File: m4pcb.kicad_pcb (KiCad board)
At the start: 2 copper layers, 26.4 x 82.3 mm, 5 parts, among them P1 CONN_01X16, P2 CONN_01X16, P3 CONN_01X16, P4 CONN_01X16, U1 STM32F415RG

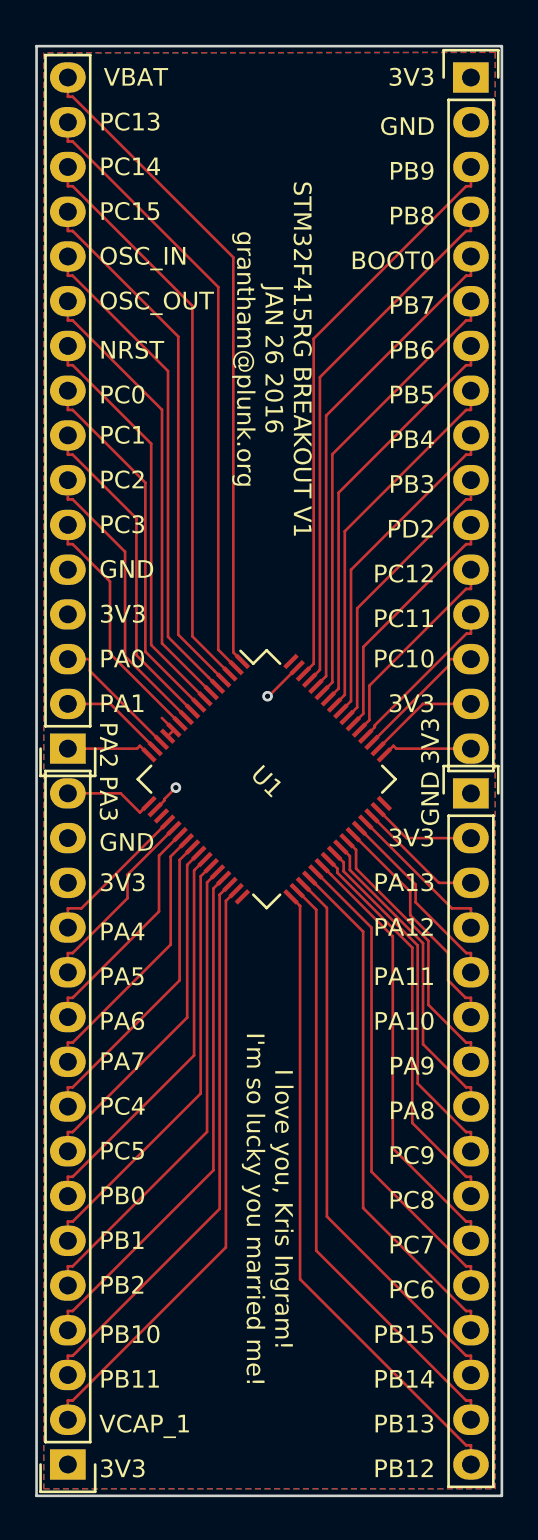
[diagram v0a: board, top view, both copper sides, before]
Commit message: narrower, would've been 2 at oshpark
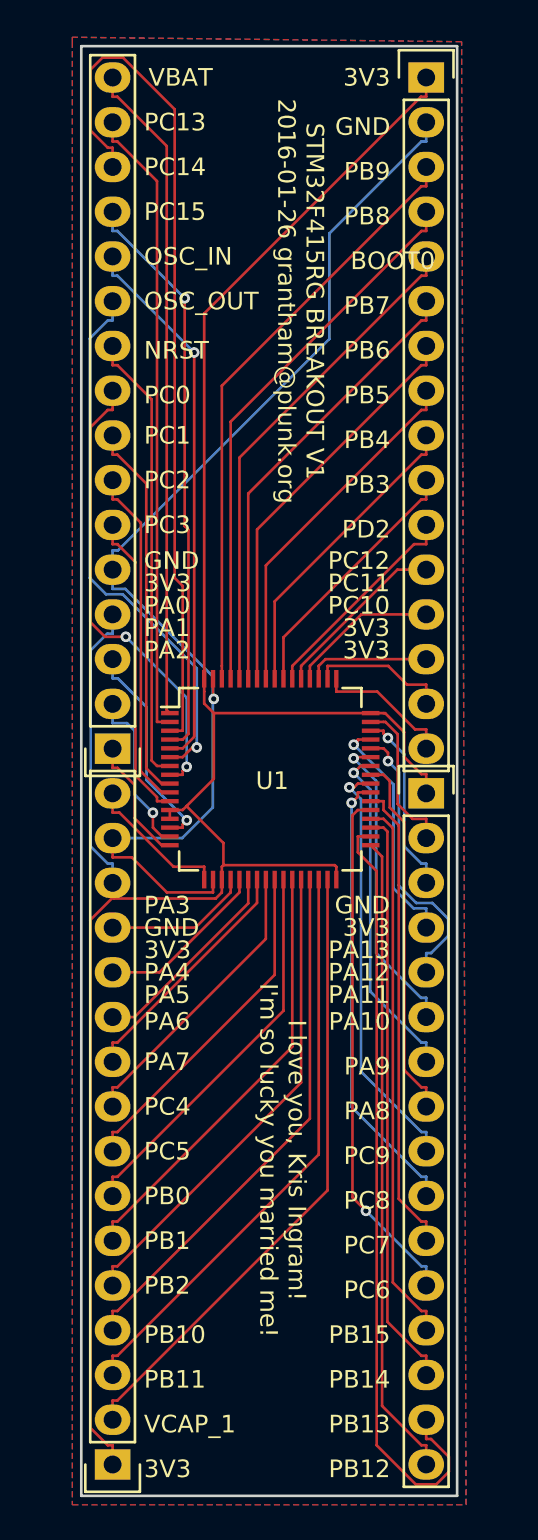
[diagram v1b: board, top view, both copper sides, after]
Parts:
- moved P1 2.54 mm to (118.1, 100.1)
- moved P2 2.54 mm to (118.1, 140.7)
- moved P3 2.54 mm to (135.9, 62.0)
- moved P4 2.54 mm to (135.9, 102.6)
- moved U1 0.20 mm to (127.1, 101.8), turned to 0 degrees
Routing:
- net 3V3: track 1.47 -> 134.8 mm
- net GND: track 4.09 -> 65.4 mm, vias 2 -> 1
- net PC14: track 32.8 -> 48.7 mm
- net PB13: track 34.3 -> 44.7 mm
- net PA11: track 10.9 -> 16.2 mm, vias 0 -> 1
- net PC0: track 21.1 -> 26.3 mm, vias 0 -> 2
- net OSC_OUT: track 25.8 -> 30.9 mm, vias 0 -> 1
- net PA0: track 7.66 -> 12.3 mm, vias 0 -> 1
- net PA12: track 9.09 -> 13.6 mm, vias 0 -> 1
- net PA10: track 13.3 -> 17.6 mm, vias 0 -> 1
- net PA9: track 15.6 -> 19.4 mm, vias 0 -> 1
- net PC9: track 20.3 -> 23.9 mm, vias 0 -> 1
- net PA1: track 6.01 -> 9.62 mm, vias 0 -> 1
- net PC3: track 14.1 -> 17.6 mm
- net PA13: track 7.19 -> 10.5 mm, vias 0 -> 1
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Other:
- board size 26.4 x 82.3 mm -> 21.3 x 82.3 mm
- board text added: "STM32F415RG BREAKOUT V1 2016-01-26 grantham@plunk.org"
- board text removed: "STM32F415RG BREAKOUT V1 JAN 26 2016 grantham@plunk.org"

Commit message: fix labels, reroute GND/3V3
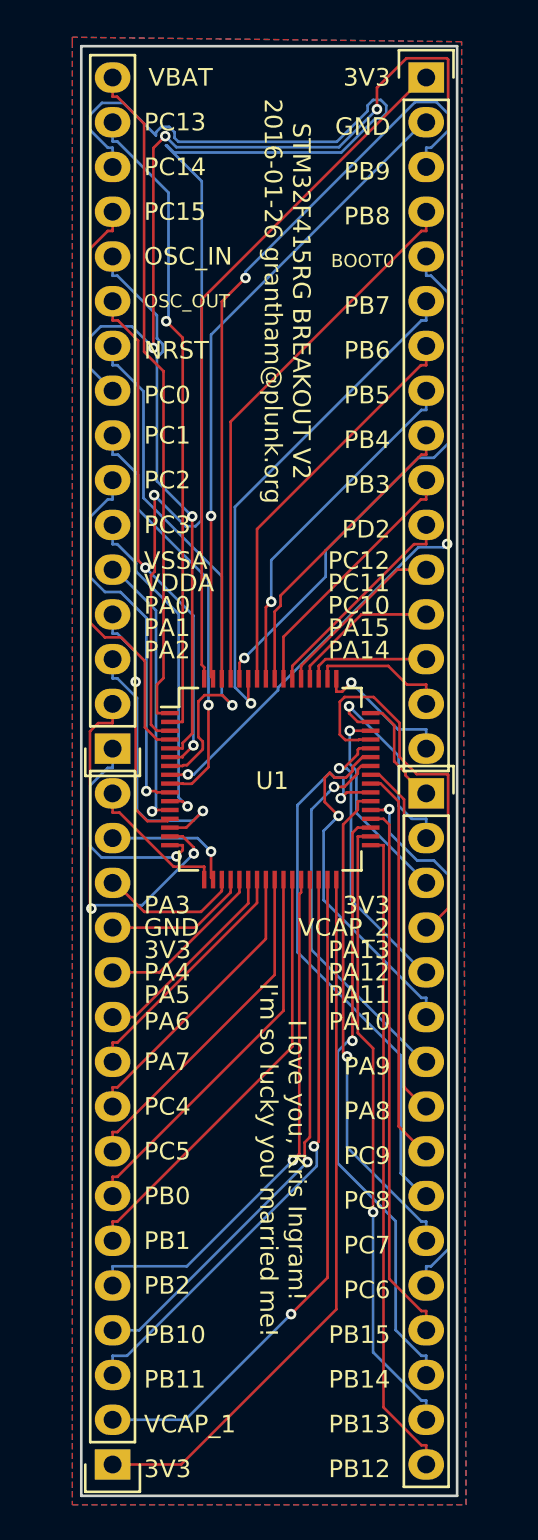
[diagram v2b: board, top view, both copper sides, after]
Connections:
- P1 pad 4: 3V3 -> VDDA
- P1 pad 5: GND -> VSSA
- U1 pad 12: 3V3 -> VSSA
- U1 pad 13: 3V3 -> VDDA
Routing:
- net PC0: track 26.3 -> 88.2 mm, vias 2 -> 5
- net 3V3: track 134.8 -> 94.7 mm
- net PC14: track 48.7 -> 77.7 mm, vias 0 -> 1
- net GND: track 65.4 -> 44.5 mm, vias 1 -> 2
- net VSSA: track 0.00 -> 16.0 mm, vias 0 -> 1
- net VDDA: track 0.00 -> 14.0 mm, vias 0 -> 1
- net PA1: track 9.62 -> 21.7 mm, vias 1 -> 2
- net PB9: track 34.0 -> 43.2 mm, vias 0 -> 1
- net PB13: track 44.7 -> 35.6 mm, vias 0 -> 1
- net PA12: track 13.6 -> 22.3 mm, vias 1 -> 0
- net PC8: track 25.7 -> 31.9 mm
- net PA2: track 7.27 -> 12.9 mm, vias 0 -> 1
- net NRST: track 25.8 -> 30.8 mm, vias 0 -> 1
- net PB7: track 25.8 -> 29.3 mm, vias 0 -> 1
- net PA0: track 12.3 -> 15.8 mm
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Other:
- board text added: "PA14"
- board text added: "PA15"
- board text added: "STM32F415RG BREAKOUT V2 2016-01-26 grantham@plunk.org"
- board text added: "VCAP_2"
- board text added: "VDDA"
- board text added: "VSSA"
- board text removed: "STM32F415RG BREAKOUT V1 2016-01-26 grantham@plunk.org"
